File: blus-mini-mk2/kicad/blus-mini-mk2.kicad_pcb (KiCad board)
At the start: 4 copper layers, 76 x 76.9 mm, 141 parts, among them J1 USB_B, J10 Conn_01x16_Female, J11 Raspberry_Pi_2_3, J12 REDFIT_SWD_10, J2 Conn_Coaxial, J4 Conn_Coaxial, J5 Screw_Terminal_01x02, J6 Screw_Terminal_01x02, J7 Screw_Terminal_01x02, J8 Screw_Terminal_01x02, J9 Screw_Terminal_01x02, SW1 BOOT, SW2 NRST, T1 DA100J, U1 TAS2780, U13 TSOP583xx, U2 TAS2780, U3 TAS2780, U4 TAS2780, U5 AMS1117-3.3, U6 STM32H743VITx, U7 TPS54302, U8 USBLC6-2SC6, U9 STM32F401RBTx, X1 ASV-24.576MHz-EJ-T

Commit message: feat: wip, added most components
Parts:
- removed C75: 4.7u, Capacitor_SMD:C_0805_2012Metric
- removed J10: Conn_01x16_Female, Connector_Debug:WR-WST REDFIT IDC 16
- removed R19: 4.7k, Resistor_SMD:R_0402_1005Metric
- removed R20: 10k, Resistor_SMD:R_0402_1005Metric
- added C64: 100n, Capacitor_SMD:C_0402_1005Metric, F.Cu at (38.6, 130.4)
- added C65: 100n, Capacitor_SMD:C_0402_1005Metric, F.Cu at (38.6, 132.4)
- added C66: 100n, Capacitor_SMD:C_0402_1005Metric, F.Cu at (38.6, 134.3)
- added C67: 100n, Capacitor_SMD:C_0402_1005Metric, F.Cu at (38.6, 136.3)
- added C68: 100n, Capacitor_SMD:C_0402_1005Metric, F.Cu at (38.6, 138.3)
- added C70: 4.7u, Capacitor_SMD:C_0805_2012Metric, F.Cu at (42.3, 130.9)
- added C71: 100n, Capacitor_SMD:C_0402_1005Metric, F.Cu at (38.6, 140.2)
- added R53: 220, Resistor_SMD:R_0402_1005Metric, F.Cu at (-56.4, 119.5)
- added R54: 100, Resistor_SMD:R_0402_1005Metric, F.Cu at (-59.4, 117.0)
- added U10: AMS1117-1.8, Package_TO_SOT_SMD:SOT-223-3_TabPin2, F.Cu at (-20.4, 82.6)
- added U11: USB3300-EZK, Package_DFN_QFN:QFN-32-1EP_5x5mm_P0.5mm_EP3.45x3.45mm, F.Cu at (-21.3, 97.5)
- added X2: ASE-24 MHz, Oscillator:Oscillator_SMD_Abracon_ASE-4Pin_3.2x2.5mm, F.Cu at (49.0, 131.6)
- C62: value 10n -> 4.7n
- R15: value 33 -> 10k
- R22: value 33 -> 12k
- U6: value STM32H743VITx -> STM32H723VGTx
- U9: value STM32F401RBTx -> 74LVC1GU04DRL; footprint Package_QFP:LQFP-64_10x10mm_P0.5mm -> Package_TO_SOT_SMD:SOT-553
- X1: value ASV-24.576MHz-EJ-T -> ASE-24.576 MHz; footprint Oscillator:Oscillator_SMD_Abracon_ASV-4Pin_7.0x5.1mm -> Oscillator:Oscillator_SMD_Abracon_ASE-4Pin_3.2x2.5mm
- moved U6 94.6 mm to (-21.1, 110.9), turned to 180 degrees
- moved X1 77.1 mm to (-74.3, 119.2), turned to 0 degrees
- moved RV1 75.4 mm to (51.6, 110.2)
- moved C76 74.1 mm to (-89.3, 96.8), turned to 180 degrees
- moved C69 72.4 mm to (-89.3, 98.8), turned to 180 degrees
- moved C94 71.2 mm to (-70.3, 118.0), turned to 0 degrees
- moved C86 70.8 mm to (-89.3, 92.9)
- moved C96 67.4 mm to (-70.3, 120.0)
- moved R35 67.3 mm to (-89.3, 82.9), turned to 180 degrees
- moved R23 65.9 mm to (47.9, 136.9), turned to 0 degrees
- moved C81 61.8 mm to (-89.3, 94.8), turned to 180 degrees
- moved C63 60.8 mm to (-89.3, 100.8), turned to 180 degrees
- moved R22 60.7 mm to (41.5, 135.4), turned to 0 degrees
- moved R15 60.2 mm to (41.5, 133.4), turned to 0 degrees
- moved R32 58.7 mm to (-83.5, 82.9), turned to 180 degrees
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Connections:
- net /Clock/CLK0 renamed /Clock/CLK_24.576
- net /PI_SDATA_I renamed /PI_SDI
- net /PI_SDATA_O renamed /PI_SD
- C62 pad 2: /SPDIF_IN -> Net-(C62-Pad2)
- J11 pad 12: /_PI_BCLK -> /PI_SCK
- J11 pad 35: /_PI_LRCLK -> /PI_FS
- J11 pad 40: /_PI_SDATA_O -> /PI_SDO
- R15 pad 1: /AMP1_BCLK -> Net-(U11-VBUS)
- R15 pad 2: /_AMP1_BCLK -> VBUS
- R16 pad 1: /EXT_LRCLKO -> /EXT_FS
- R16 pad 2: /_EXT_LRCLKO -> /MCU/SAI1_FS_A
- R22 pad 1: /AMP1_SDIN -> GND
- R22 pad 2: /_AMP1_SDIN -> Net-(U11-RBIAS)
- R23 pad 1: /AMP1_LRCLK -> /USB_CLK
- R23 pad 2: /_AMP1_LRCLK -> /Clock/CLK_24.000
- R24 pad 1: /EXT_MDO -> /EXT_SD
- R24 pad 2: /_EXT_MDO -> /MCU/SAI1_SD_A
- R25 pad 1: /EXT_BCLKO -> /EXT_SCK
- R25 pad 2: /_EXT_BCLKO -> /MCU/SAI1_SCK_A
- R28 pad 1: /USB_BCLK -> /Amplifiers/SCLKA
- R28 pad 2: /MCU/I2S3_SCK -> /MCU/SAI4_SCK_A
- R30 pad 1: /USB_LRCLK -> /Amplifiers/LRCKA
- R30 pad 2: /MCU/I2S3_WS -> /MCU/SAI4_FS_A
- R33 pad 1: /USB_SDATA -> /Amplifiers/SDINA
- R33 pad 2: /MCU/I2S3_SD -> /MCU/SAI4_SD_A
- R38 pad 1: /MCU_CLOCK -> /AUDIO_CLK
- R41 pad 1: /_PI_SDATA_O -> /MCU/SAI4_SD_B
- R42 pad 1: /_PI_LRCLK -> /MCU/SAI4_FS_B
- R42 pad 2: /PI_LRCLK -> /PI_FS
- R43 pad 1: /_PI_BCLK -> /MCU/SAI4_SCK_B
- R43 pad 2: /PI_BCLK -> /PI_SCK
- U1 pad 13: /AMP1_SDIN -> /Amplifiers/SDINA
- U1 pad 14: /AMP1_LRCLK -> /Amplifiers/LRCKA
- U1 pad 15: /AMP1_BCLK -> /Amplifiers/SCLKA
- U2 pad 13: /AMP1_SDIN -> /Amplifiers/SDINA
- U2 pad 14: /AMP1_LRCLK -> /Amplifiers/LRCKA
- U2 pad 15: /AMP1_BCLK -> /Amplifiers/SCLKA
- U3 pad 13: /AMP1_SDIN -> /Amplifiers/SDINA
- U3 pad 14: /AMP1_LRCLK -> /Amplifiers/LRCKA
- U3 pad 15: /AMP1_BCLK -> /Amplifiers/SCLKA
- U4 pad 13: /AMP1_SDIN -> /Amplifiers/SDINA
- U4 pad 14: /AMP1_LRCLK -> /Amplifiers/LRCKA
- U4 pad 15: /AMP1_BCLK -> /Amplifiers/SCLKA
- U6 pad 15: unconnected-(U6-PC0-Pad15) -> /MCU/ULPI_STP
- U6 pad 16: unconnected-(U6-PC1-Pad16) -> /MCU/SAI4_SD_A
- U6 pad 17: unconnected-(U6-PC2_C-Pad17) -> /MCU/ULPI_DIR
- U6 pad 18: unconnected-(U6-PC3_C-Pad18) -> /MCU/ULPI_NXT
- U6 pad 2: unconnected-(U6-PE3-Pad2) -> /SPDIF_OUT
- U6 pad 22: unconnected-(U6-PA0-Pad22) -> /MCU/SAI4_SD_B
- U6 pad 24: unconnected-(U6-PA2-Pad24) -> /MCU/SAI4_SCK_B
- U6 pad 25: unconnected-(U6-PA3-Pad25) -> /MCU/ULPI_D0
- U6 pad 29: unconnected-(U6-PA5-Pad29) -> /MCU/ULPI_CK
- U6 pad 3: unconnected-(U6-PE4-Pad3) -> /MCU/SAI1_FS_A
- U6 pad 34: unconnected-(U6-PB0-Pad34) -> /MCU/ULPI_D1
- U6 pad 35: unconnected-(U6-PB1-Pad35) -> /MCU/ULPI_D2
- U6 pad 37: unconnected-(U6-PE7-Pad37) -> /MCU/TIM1_ETR
- U6 pad 4: unconnected-(U6-PE5-Pad4) -> /MCU/SAI1_SCK_A
- U6 pad 43: unconnected-(U6-PE13-Pad43) -> /MCU/SAI4_FS_B
- U6 pad 46: unconnected-(U6-PB10-Pad46) -> /MCU/ULPI_D3
- U6 pad 47: unconnected-(U6-PB11-Pad47) -> /MCU/ULPI_D4
- U6 pad 5: unconnected-(U6-PE6-Pad5) -> /MCU/SAI1_SD_A
- U6 pad 51: unconnected-(U6-PB12-Pad51) -> /MCU/ULPI_D5
- U6 pad 52: unconnected-(U6-PB13-Pad52) -> /MCU/ULPI_D6
- U6 pad 55: unconnected-(U6-PD8-Pad55) -> /MCU/SPDIF_IN1
- U6 pad 59: unconnected-(U6-PD12-Pad59) -> /MCU/SAI4_FS_A
- U6 pad 60: unconnected-(U6-PD13-Pad60) -> /MCU/SAI4_SCK_A
- U6 pad 67: unconnected-(U6-PA8-Pad67) -> /MCU/TIM1_ETR
- U6 pad 72: unconnected-(U6-PA13-Pad72) -> /MCU/TMS
- U6 pad 76: unconnected-(U6-PA14-Pad76) -> /MCU/TCK
- U6 pad 88: unconnected-(U6-PD7-Pad88) -> /SPDIF_IN0
- U6 pad 89: unconnected-(U6-PB3-Pad89) -> /MCU/SWO
- U6 pad 91: unconnected-(U6-PB5-Pad91) -> /MCU/ULPI_D7
- U6 pad 97: unconnected-(U6-PE0-Pad97) -> /AUDIO_CLK
- U9 pad 1: +3.3V -> unconnected-(U9-NC-Pad1)
- U9 pad 2: unconnected-(U9-PC13-Pad2) -> Net-(R53-Pad2)
- U9 pad 3: unconnected-(U9-PC14-Pad3) -> GND
- U9 pad 4: unconnected-(U9-PC15-Pad4) -> /SPDIF_IN
- U9 pad 5: /MCU_CLOCK -> Net-(U9-VCC)
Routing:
- net /AMP1_SDIN: track 122.7 -> 0.00 mm, vias 5 -> 0
- net /AMP1_LRCLK: track 117.3 -> 0.00 mm, vias 5 -> 0
- net /AMP1_BCLK: track 111.2 -> 0.00 mm, vias 5 -> 0
- net /SCL: track 158.3 -> 64.7 mm, vias 6 -> 4
- net /SDA: track 157.6 -> 68.8 mm, vias 6 -> 4
- net PI_3V3: track 52.0 -> 0.00 mm
- net /IR_INPUT: track 50.9 -> 0.00 mm, vias 1 -> 0
- net +3.3V: track 70.0 -> 32.4 mm, vias 21 -> 8
- net /EXT_MDO: track 31.7 -> 0.00 mm
- net /MCU/NRST: track 30.3 -> 0.00 mm, vias 1 -> 0
- net /EXT_LRCLKO: track 28.8 -> 0.00 mm
- net /Amplifiers/NSPK_SD: track 81.7 -> 54.0 mm
- net /EXT_BCLKO: track 27.1 -> 0.00 mm
- net /MCU/BOOT0: track 23.1 -> 0.00 mm, vias 2 -> 0
- net /MCU_CLOCK: track 21.9 -> 0.00 mm, vias 2 -> 0
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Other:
- board size 76 x 76.9 mm -> 66.5 x 76.9 mm

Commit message: feat: production version, blus mini mk2 a
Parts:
- removed the C66 at (38.6, 134.3)
- removed the C67 at (38.6, 136.3)
- removed the C68 at (38.6, 138.3)
- removed the C69 at (-89.3, 98.8)
- removed the C70 at (42.3, 130.9)
- removed the C71 at (38.6, 140.2)
- removed the C76 at (-89.3, 96.8)
- removed the C81 at (-89.3, 94.8)
- removed C94: 10n, Capacitor_SMD:C_0402_1005Metric
- removed C96: 100n, Capacitor_SMD:C_0402_1005Metric
- removed the J1 at (-30.6, 81.4)
- removed the R15 at (41.5, 133.4)
- removed the R16 at (-27.8, 120.1)
- removed the R17 at (-29.0, 97.4)
- removed the R22 at (41.5, 135.4)
- removed the R33 at (-21.6, 116.2)
- removed the R35 at (-89.3, 82.9)
- removed the R38 at (-33.1, 114.1)
- removed the R43 at (-4.75, 124.9)
- removed R53: 220, Resistor_SMD:R_0402_1005Metric
- removed R54: 100, Resistor_SMD:R_0402_1005Metric
- removed the U11 at (-21.3, 97.5)
- removed U13: TSOP583xx, OptoDevice:Vishay_MINICAST-3Pin
- removed the U9 at (-62.2, 118.8)
- removed oshw1: Logo_Open_Hardware_Large, Symbol:OSHW-Symbol_6.7x6mm_SilkScreen
- added C1: 100n, Capacitor_SMD:C_0402_1005Metric, F.Cu at (149.4, 100.5)
- added C2: 10n, Capacitor_SMD:C_0402_1005Metric, F.Cu at (149.4, 99.4)
- added C3: 100n, Capacitor_SMD:C_0402_1005Metric, F.Cu at (120.6, 100.5)
- added C4: 10n, Capacitor_SMD:C_0402_1005Metric, F.Cu at (119.6, 100.5)
- added C44: 4.7n, Capacitor_SMD:C_0402_1005Metric, F.Cu at (158.2, 117.1)
- added C46: 4.7u, Capacitor_SMD:C_0805_2012Metric, F.Cu at (120.1, 106.7)
- added C47: 100n, Capacitor_SMD:C_0402_1005Metric, F.Cu at (127.1, 103.9)
- added C48: 4.7u, Capacitor_SMD:C_0805_2012Metric, F.Cu at (124.2, 103.6)
- added C49: 100n, Capacitor_SMD:C_0402_1005Metric, F.Cu at (128.6, 103.9)
- added C50: 4.7u, Capacitor_SMD:C_0805_2012Metric, F.Cu at (131.0, 103.0)
- added C51: 100n, Capacitor_SMD:C_0402_1005Metric, F.Cu at (130.9, 112.0)
- added C52: 100n, Capacitor_SMD:C_0402_1005Metric, F.Cu at (123.4, 108.6)
- added C53: 100n, Capacitor_SMD:C_0402_1005Metric, F.Cu at (131.9, 105.6)
- added C54: 100n, Capacitor_SMD:C_0402_1005Metric, F.Cu at (123.4, 105.3)
- added C55: 4.7u, Capacitor_SMD:C_0805_2012Metric, F.Cu at (135.1, 119.9)
- added C56: 4.7u, Capacitor_SMD:C_0805_2012Metric, F.Cu at (150.6, 124.1)
- added C57: 4.7u, Capacitor_SMD:C_0805_2012Metric, F.Cu at (139.5, 102.6)
- added C58: 100n, Capacitor_SMD:C_0402_1005Metric, F.Cu at (153.1, 122.1)
- added C59: 100n, Capacitor_SMD:C_0402_1005Metric, F.Cu at (146.8, 103.8)
- added D1: Blue, LED_SMD:LED_0603_1608Metric, F.Cu at (136.5, 127.4)
- added D2: Green, LED_SMD:LED_0603_1608Metric, F.Cu at (136.5, 129.1)
- added D3: Yellow, LED_SMD:LED_0603_1608Metric, F.Cu at (136.5, 130.9)
- added D4: Red, LED_SMD:LED_0603_1608Metric, F.Cu at (136.5, 132.6)
- added J3: Conn_02x08_Odd_Even, Connector_IDC:IDC-Header_2x08_P2.54mm_Horizontal, B.Cu at (179.9, 121.1)
- added J7: USB_B, Connector_USB:USB_B_TE_5787834_Vertical, F.Cu at (126.5, 117.0)
- added JP1: SolderJumper_3_Bridged12, Jumper:SolderJumper-3_P1.3mm_Bridged12_RoundedPad1.0x1.5mm, F.Cu at (153.1, 101.9)
- added R1: 33, Resistor_SMD:R_0402_1005Metric, F.Cu at (145.6, 102.8)
- added R11: 33, Resistor_SMD:R_0402_1005Metric, F.Cu at (154.4, 103.8)
- added R12: 33, Resistor_SMD:R_0402_1005Metric, F.Cu at (154.4, 104.9)
- added R13: 33, Resistor_SMD:R_0402_1005Metric, F.Cu at (154.4, 106.0)
- added R14: 33, Resistor_SMD:R_0402_1005Metric, F.Cu at (152.2, 100.0)
- added R19: 220, Resistor_SMD:R_0402_1005Metric, F.Cu at (158.2, 116.0)
- added R2: 33, Resistor_SMD:R_0402_1005Metric, F.Cu at (125.6, 102.0)
- added R26: 330, Resistor_SMD:R_0402_1005Metric, F.Cu at (139.1, 128.2)
- added R27: 330, Resistor_SMD:R_0402_1005Metric, F.Cu at (139.1, 129.4)
- added R29: 330, Resistor_SMD:R_0402_1005Metric, F.Cu at (139.1, 131.8)
- added R31: 4.7k, Resistor_SMD:R_0402_1005Metric, F.Cu at (144.4, 93.6)
- added R5: 33, Resistor_SMD:R_0402_1005Metric, F.Cu at (144.1, 124.1)
- added R6: 33, Resistor_SMD:R_0402_1005Metric, F.Cu at (143.0, 124.1)
- added R7: 33, Resistor_SMD:R_0402_1005Metric, F.Cu at (143.9, 103.8)
- added R8: 33, Resistor_SMD:R_0402_1005Metric, F.Cu at (160.1, 133.2)
- added U1: TSOP583xx, OptoDevice:Vishay_MINICAST-3Pin, F.Cu at (189.9, 140.0)
- added U5: 74LVC1GU04DRL, Package_TO_SOT_SMD:SOT-553, F.Cu at (155.8, 116.0)
- added U7: USB3300-EZK, Package_DFN_QFN:QFN-32-1EP_5x5mm_P0.5mm_EP3.45x3.45mm, F.Cu at (127.7, 108.2)
- C60, C61: value 4.7u -> 100n; footprint Capacitor_SMD:C_0805_2012Metric -> Capacitor_SMD:C_0402_1005Metric
- C62: value 4.7n -> 100n
- R18: value 33 -> 100
- R25: value 33 -> 10k
- R28: value 33 -> 330
- R30: value 33 -> 12k
- U6: value STM32H723VGTx -> USBLC6-2SC6; footprint Package_QFP:LQFP-100_14x14mm_P0.5mm -> Package_TO_SOT_SMD:SOT-23-6
- U8: value USBLC6-2SC6 -> STM32H723VGTx; footprint Package_TO_SOT_SMD:SOT-23-6 -> Package_QFP:LQFP-100_14x14mm_P0.5mm
- moved C86 246.0 mm to (155.5, 117.8), turned to 0 degrees
- moved C60 228.6 mm to (135.8, 107.9), turned to 90 degrees
- moved R32 228.0 mm to (144.4, 87.5), turned to 90 degrees
- moved C63 227.8 mm to (137.5, 122.1), turned to 0 degrees
- moved C61 224.7 mm to (142.1, 104.2), turned to 0 degrees
- moved R4 222.4 mm to (177.5, 108.2), turned to 90 degrees
- moved R3 222.2 mm to (177.5, 106.2), turned to -90 degrees
- moved X1 221.4 mm to (146.3, 99.9), turned to 180 degrees
- moved J6 204.9 mm to (167.7, 102.0), turned to 0 degrees
- moved U10 201.8 mm to (188.8, 86.9), turned to 0 degrees
- moved U11 199.4 mm to (178.7, 94.9), turned to 0 degrees
- moved SW2 194.6 mm to (149.2, 95.0), turned to 180 degrees
- moved SW1 194.4 mm to (149.2, 88.9), turned to 0 degrees
- moved R18 185.4 mm to (155.5, 114.2), turned to 180 degrees
- moved U8 178.6 mm to (145.4, 113.9), turned to -90 degrees
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- renumbered C52 to C10, C39 to C11, C44 to C12, C51 to C13, C24 to C14, C8 to C15, C7 to C16, C15 to C17, C19 to C18, C12 to C19, C36 to C20, C26 to C21, C30 to C22, C48 to C23, C35 to C24, C42 to C25, C47 to C26, C20 to C27, C4 to C28, C3 to C29, C11 to C30, C17 to C31, C10 to C32, C34 to C33, C25 to C34, C29 to C35, C46 to C36, C33 to C37, C41 to C38, C45 to C39, C18 to C40, C2 to C41, C1 to C42, C9 to C43, C97 to C45, C23 to C5, C16 to C6, C54 to C66, C53 to C67, C55 to C68, C59 to C69, C40 to C7, C58 to C70, C57 to C71, C56 to C72, C21 to C73, C14 to C74, C38 to C75, C27 to C76, C31 to C77, C50 to C78, C37 to C79, C28 to C8, C43 to C80, C49 to C81, C22 to C82, C6 to C83, C5 to C84, C13 to C85, C32 to C9, H2 to H1, H1 to H2, J9 to J1, J7 to J10, J8 to J11, J11 to J2, J2 to J4, J4 to J5, J12 to J6, J5 to J8, J6 to J9, R41 to R10, R4 to R15, R2 to R16, R1 to R17, R44 to R20, R45 to R22, R27 to R3, R12 to R33, R11 to R34, R14 to R35, R10 to R36, R13 to R37, R5 to R38, R9 to R39, R29 to R4, R8 to R40, R7 to R41, R6 to R42, R3 to R43, R42 to R9, U5 to U10, U10 to U11, U3 to U12, U4 to U2, U2 to U3, U1 to U4, U7 to U9
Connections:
- net /Amplifiers/SDINA renamed /Amplifiers/TDM_SDI
- C60 pad 1: Net-(C60-Pad1) -> +3.3V
- C61 pad 1: Net-(C61-Pad1) -> +3.3V
- C62 pad 1: Net-(J2-In) -> +3.3V
- C62 pad 2: Net-(C62-Pad2) -> GND
- J2 pad 1: PI_3V3 -> unconnected-(J2-3V3-Pad1)_0
- J2 pad 11: /DSP_NRESET -> unconnected-(J2-GPIO17-Pad11)
- J2 pad 15: /DSP_SELFBOOT -> unconnected-(J2-GPIO22-Pad15)
- J2 pad 23: /PI_SCLK0 -> /PI_TDM_SCK0
- J4 pad 1: Net-(J2-In) -> Net-(J4-In)
- J6 pad 8: unconnected-(J12-TDI-Pad8) -> /MCU/TDI
- R10 pad 2: /PI_SD -> /PI_SDO
- R18 pad 2: /MCU/USB_DM -> /SPDIF_IN
- R21 pad 1: Net-(J2-In) -> Net-(J4-In)
- R23 pad 1: /USB_CLK -> Net-(R23-Pad1)
- R23 pad 2: /Clock/CLK_24.000 -> /MCU/USB_DN
- R24 pad 1: /EXT_SD -> Net-(R24-Pad1)
- R24 pad 2: /MCU/SAI1_SD_A -> /MCU/USB_DP
- R25 pad 1: /EXT_SCK -> Net-(U7-VBUS)
- R25 pad 2: /MCU/SAI1_SCK_A -> VBUS
- R28 pad 1: /Amplifiers/SCLKA -> Net-(D3-A)
- R28 pad 2: /MCU/SAI4_SCK_A -> /MCU/LED3
- R30 pad 1: /Amplifiers/LRCKA -> GND
- R30 pad 2: /MCU/SAI4_FS_A -> Net-(U7-RBIAS)
- RV1 pad 1: /AVDD -> +3.3V
- U12 pad 14: /Amplifiers/LRCKA -> /Amplifiers/TDM_FS
- U12 pad 15: /Amplifiers/SCLKA -> /Amplifiers/TDM_SCK
- U12 pad 22: /Amplifiers/NSPK_SD -> /Amplifiers/~{SPK_SD}
- U2 pad 14: /Amplifiers/LRCKA -> /Amplifiers/TDM_FS
- U2 pad 15: /Amplifiers/SCLKA -> /Amplifiers/TDM_SCK
- U2 pad 22: /Amplifiers/NSPK_SD -> /Amplifiers/~{SPK_SD}
- U3 pad 14: /Amplifiers/LRCKA -> /Amplifiers/TDM_FS
- U3 pad 15: /Amplifiers/SCLKA -> /Amplifiers/TDM_SCK
- U3 pad 22: /Amplifiers/NSPK_SD -> /Amplifiers/~{SPK_SD}
- U4 pad 14: /Amplifiers/LRCKA -> /Amplifiers/TDM_FS
- U4 pad 15: /Amplifiers/SCLKA -> /Amplifiers/TDM_SCK
- U4 pad 22: /Amplifiers/NSPK_SD -> /Amplifiers/~{SPK_SD}
- U6 pad 1: unconnected-(U6-PE2-Pad1) -> /MCU/_USB_DN
- U6 pad 2: /SPDIF_OUT -> GND
- U6 pad 3: /MCU/SAI1_FS_A -> /MCU/_USB_DP
- U6 pad 4: /MCU/SAI1_SCK_A -> Net-(R24-Pad1)
- U6 pad 5: /MCU/SAI1_SD_A -> VBUS
- U6 pad 6: +3.3V -> Net-(R23-Pad1)
- U8 pad 1: Net-(J1-D-) -> /MCU/SAI1_MCLK_A
- U8 pad 2: GND -> /SPDIF_OUT
- U8 pad 3: Net-(J1-D+) -> /MCU/SAI1_FS_A
- U8 pad 4: Net-(R17-Pad1) -> /MCU/SAI1_SCK_A
- U8 pad 5: VBUS -> /MCU/SAI1_SD_A
- U8 pad 6: Net-(R18-Pad1) -> +3.3V
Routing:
- net /Amplifiers/TDM_FS: track 0.00 -> 122.5 mm, vias 0 -> 5
- net /Amplifiers/TDM_SCK: track 0.00 -> 119.1 mm, vias 0 -> 5
- net /Amplifiers/TDM_SDI: track 0.00 -> 104.3 mm, vias 0 -> 5
- net /Amplifiers/~{SPK_SD}: track 0.00 -> 97.3 mm, vias 0 -> 6
- net +3.3V: track 32.4 -> 114.0 mm, vias 8 -> 33
- net /SCL: track 64.7 -> 132.8 mm, vias 4 -> 6
- net /SDA: track 68.8 -> 133.4 mm, vias 4 -> 6
- net /IR_INPUT: track 0.00 -> 58.8 mm
- net /Amplifiers/NSPK_SD: track 54.0 -> 0.00 mm, vias 4 -> 0
- net /MCU/NRST: track 0.00 -> 44.7 mm
- net /EXT_SDO: track 0.00 -> 36.2 mm, vias 0 -> 1
- net /EXT_SDI: track 0.00 -> 35.6 mm, vias 0 -> 1
- net /MCU/SAI4_SCK_B: track 0.00 -> 34.4 mm, vias 0 -> 2
- net /MCU/BOOT0: track 0.00 -> 33.8 mm, vias 0 -> 2
- net /EXT_SCK: track 0.00 -> 32.6 mm
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- removed copper zone on F.Cu, net Net-(U12-BST_N)
- removed copper zone on F.Cu, net Net-(U12-BST_P)
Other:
- board size 66.5 x 76.9 mm -> 76.5 x 76.9 mm
- board text added: "1V8"
- board text added: "3V3"
- board text added: "M2.5x4"
- board text added: "VOL"
- board text added: "blus mini mk2"
- board text added: "out/in"
- board text added: "rev a af 24"
- board text removed: "DSP ADC0"
- board text removed: "MCU ADC1_9"
- board text removed: "PI M2.5x4"
- board text removed: "blus mini af 23"
- board text removed: "rev b"

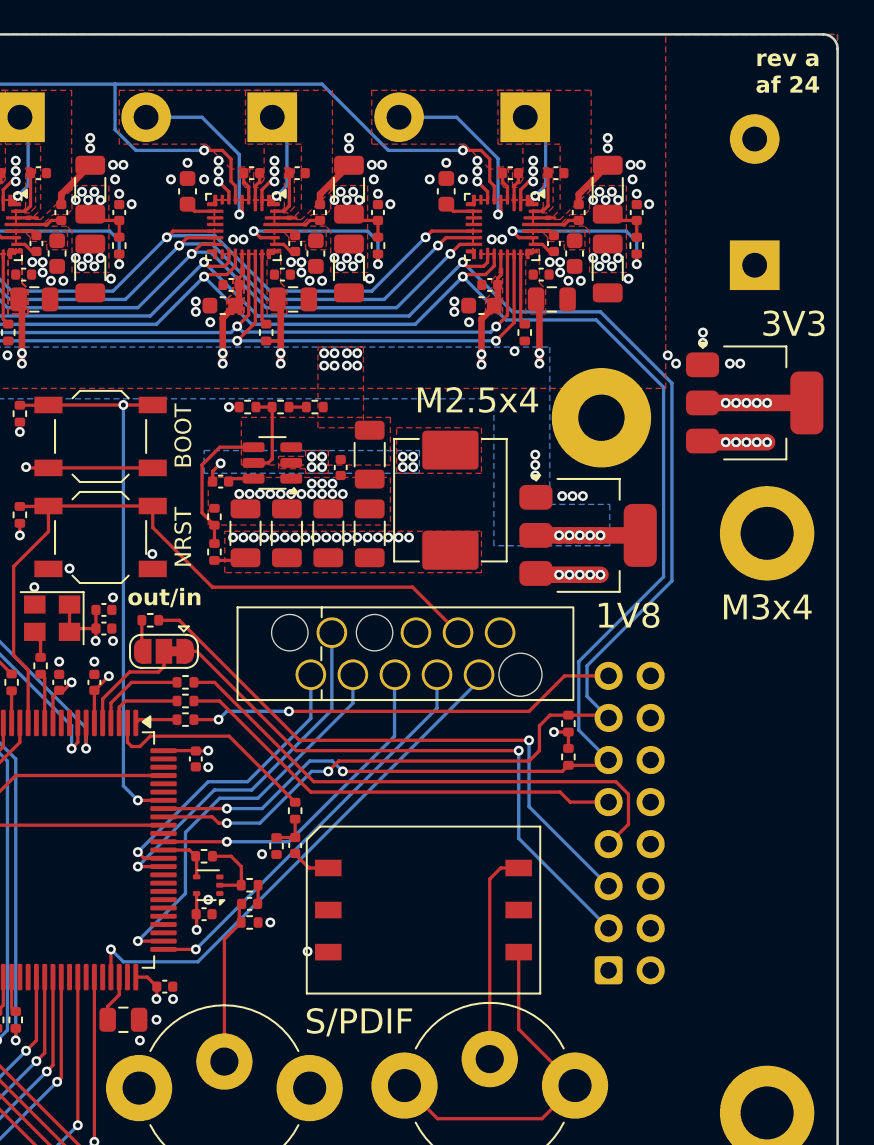
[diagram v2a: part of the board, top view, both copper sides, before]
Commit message: fix: update to rev b, capacitor location
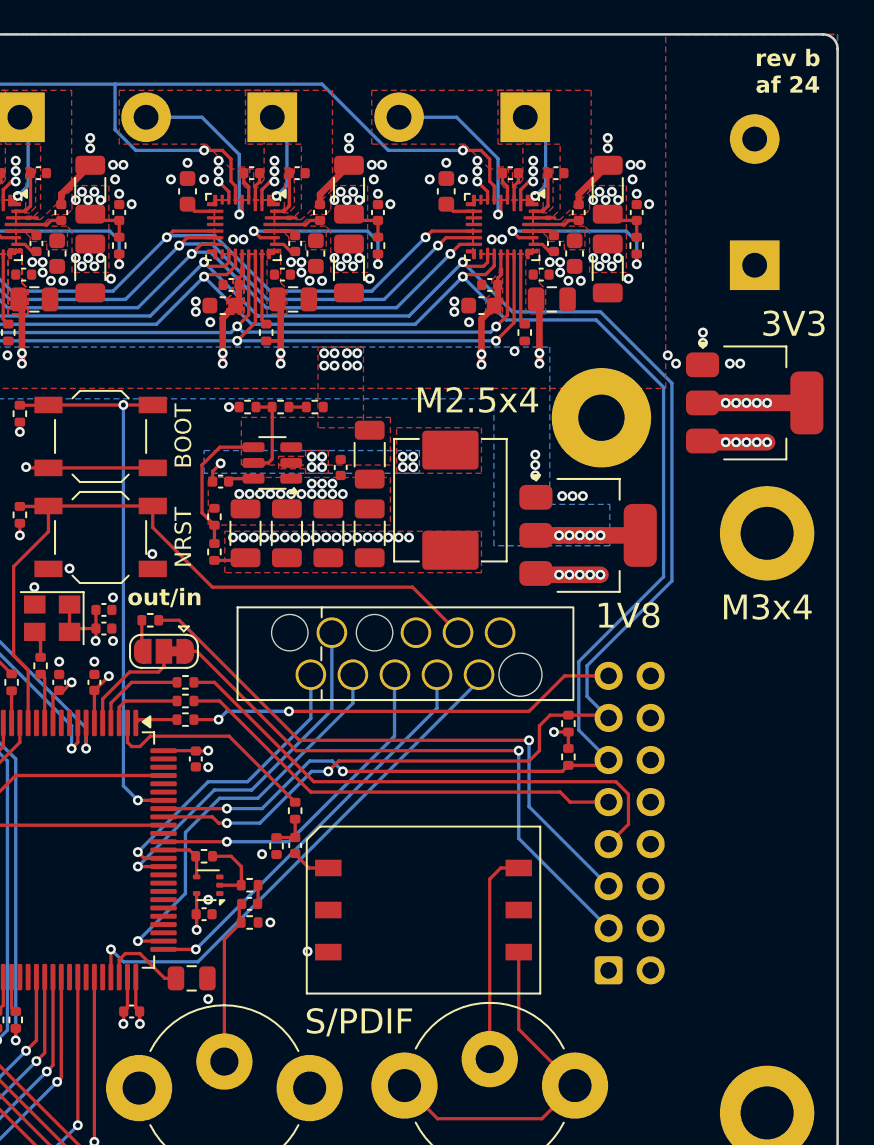
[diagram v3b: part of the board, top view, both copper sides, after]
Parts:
- moved C56 4.82 mm to (154.8, 121.6)
- moved C58 2.50 mm to (151.1, 123.6), turned to 180 degrees
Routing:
- net GND: track 33.7 -> 36.6 mm, vias 184 -> 183
- net Net-(C56-Pad1): track 2.86 -> 5.25 mm
- net +3.3V: track 114.0 -> 114.7 mm
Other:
- board text added: "rev b af 24"
- board text removed: "rev a af 24"
